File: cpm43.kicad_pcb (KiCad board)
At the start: 2 copper layers, 232.2 x 76.7 mm, 185 parts, among them Q1 Q_NPN_BCE, SW1 SW_PUSH, U1 ATmega32U4, U2 PRTR5V0U2X

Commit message: Tact switch
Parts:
- SW1: footprint Keebio-Parts:CandK_6x6mm_Tactile -> Buttons_Switches_SMD:SW_SPST_TL3342
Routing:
- net GND: track 114.4 -> 120.7 mm, vias 167 -> 169
- net RST: track 178.8 -> 181.2 mm, vias 5 -> 7
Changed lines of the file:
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@@
     (thickness 1.6)
     (drawings 49)
-    (tracks 2415)
+    (tracks 2423)
     (zones 0)
     (modules 185)
@@
     (add_net VCC)
   )
+  (module Buttons_Switches_SMD:SW_SPST_TL3342 (layer B.Cu)
+    (at 233.3244 85.852 270)
+    (descr "Low-profile SMD Tactile Switch, https://www.e-switch.com/system/asset/product_line/data_sheet/165/TL3342.pdf")
+    (tags "SPST Tactile Switch")
+    (attr smd)
+    (fp_text reference SW1 (at 0 3.75 270) (layer B.SilkS)
+      (effects (font (size 1 1) (thickness 0.15)) (justify mirror))
+    )
+    (fp_text value SW_PUSH (at 0 -3.75 270) (layer B.Fab)
+      (effects (font (size 1 1) (thickness 0.15)) (justify mirror))
+    )
+    (fp_text user %R (at 0 3.75 270) (layer B.Fab)
+      (effects (font (size 1 1) (thickness 0.15)) (justify mirror))
+    )
+    (fp_line (start 3.2 -2.1) (end 3.2 -1.6) (layer B.Fab) (width 0.1))
+    (fp_line (start 3.2 2.1) (end 3.2 1.6) (layer B.Fab) (width 0.1))
+    (fp_line (start -3.2 -2.1) (end -3.2 -1.6) (layer B.Fab) (width 0.1))
+    (fp_line (start -3.2 2.1) (end -3.2 1.6) (layer B.Fab) (width 0.1))
+    (fp_line (start 2.7 2.1) (end 2.7 1.6) (layer B.Fab) (width 0.1))
+    (fp_line (start 1.7 2.1) (end 3.2 2.1) (layer B.Fab) (width 0.1))
+    (fp_line (start 3.2 1.6) (end 2.2 1.6) (layer B.Fab) (width 0.1))
+    (fp_line (start -2.7 2.1) (end -2.7 1.6) (layer B.Fab) (width 0.1))
+    (fp_line (start -1.7 2.1) (end -3.2 2.1) (layer B.Fab) (width 0.1))
+    (fp_line (start -3.2 1.6) (end -2.2 1.6) (layer B.Fab) (width 0.1))
+    (fp_line (start -2.7 -2.1) (end -2.7 -1.6) (layer B.Fab) (width 0.1))
+    (fp_line (start -3.2 -1.6) (end -2.2 -1.6) (layer B.Fab) (width 0.1))
+    (fp_line (start -1.7 -2.1) (end -3.2 -2.1) (layer B.Fab) (width 0.1))
+    (fp_line (start 1.7 -2.1) (end 3.2 -2.1) (layer B.Fab) (width 0.1))
+    (fp_line (start 2.7 -2.1) (end 2.7 -1.6) (layer B.Fab) (width 0.1))
+    (fp_line (start 3.2 -1.6) (end 2.2 -1.6) (layer B.Fab) (width 0.1))
+    (fp_line (start -1.7 -2.3) (end -1.25 -2.75) (layer B.SilkS) (width 0.12))
+    (fp_line (start 1.7 -2.3) (end 1.25 -2.75) (layer B.SilkS) (width 0.12))
+    (fp_line (start 1.7 2.3) (end 1.25 2.75) (layer B.SilkS) (width 0.12))
+    (fp_line (start -1.7 2.3) (end -1.25 2.75) (layer B.SilkS) (width 0.12))
+    (fp_line (start -2 1) (end -1 2) (layer B.Fab) (width 0.1))
+    (fp_line (start -1 2) (end 1 2) (layer B.Fab) (width 0.1))
+    (fp_line (start 1 2) (end 2 1) (layer B.Fab) (width 0.1))
+    (fp_line (start 2 1) (end 2 -1) (layer B.Fab) (width 0.1))
+    (fp_line (start 2 -1) (end 1 -2) (layer B.Fab) (width 0.1))
+    (fp_line (start 1 -2) (end -1 -2) (layer B.Fab) (width 0.1))
+    (fp_line (start -1 -2) (end -2 -1) (layer B.Fab) (width 0.1))
+    (fp_line (start -2 -1) (end -2 1) (layer B.Fab) (width 0.1))
+    (fp_line (start 2.75 1) (end 2.75 -1) (layer B.SilkS) (width 0.12))
+    (fp_line (start -1.25 -2.75) (end 1.25 -2.75) (layer B.SilkS) (width 0.12))
+    (fp_line (start -2.75 1) (end -2.75 -1) (layer B.SilkS) (width 0.12))
+    (fp_line (start -1.25 2.75) (end 1.25 2.75) (layer B.SilkS) (width 0.12))
+    (fp_line (start -2.6 1.2) (end -2.6 -1.2) (layer B.Fab) (width 0.1))
+    (fp_line (start -2.6 -1.2) (end -1.2 -2.6) (layer B.Fab) (width 0.1))
+    (fp_line (start -1.2 -2.6) (end 1.2 -2.6) (layer B.Fab) (width 0.1))
+    (fp_line (start 1.2 -2.6) (end 2.6 -1.2) (layer B.Fab) (width 0.1))
+    (fp_line (start 2.6 -1.2) (end 2.6 1.2) (layer B.Fab) (width 0.1))
+    (fp_line (start 2.6 1.2) (end 1.2 2.6) (layer B.Fab) (width 0.1))
+    (fp_line (start 1.2 2.6) (end -1.2 2.6) (layer B.Fab) (width 0.1))
+    (fp_line (start -1.2 2.6) (end -2.6 1.2) (layer B.Fab) (width 0.1))
+    (fp_line (start -4.25 3) (end 4.25 3) (layer B.CrtYd) (width 0.05))
+    (fp_line (start 4.25 3) (end 4.25 -3) (layer B.CrtYd) (width 0.05))
+    (fp_line (start 4.25 -3) (end -4.25 -3) (layer B.CrtYd) (width 0.05))
+    (fp_line (start -4.25 -3) (end -4.25 3) (layer B.CrtYd) (width 0.05))
+    (fp_circle (center 0 0) (end 1 0) (layer B.Fab) (width 0.1))
+    (pad 1 smd rect (at -3.15 1.9 270) (size 1.7 1) (layers B.Cu B.Paste B.Mask)
+      (net 2 GND))
+    (pad 1 smd rect (at 3.15 1.9 270) (size 1.7 1) (layers B.Cu B.Paste B.Mask)
+      (net 2 GND))
+    (pad 2 smd rect (at -3.15 -1.9 270) (size 1.7 1) (layers B.Cu B.Paste B.Mask)
+      (net 126 RST))
+    (pad 2 smd rect (at 3.15 -1.9 270) (size 1.7 1) (layers B.Cu B.Paste B.Mask)
+      (net 126 RST))
+    (model ${KISYS3DMOD}/Buttons_Switches_SMD.3dshapes/SW_SPST_TL3342.wrl
+      (at (xyz 0 0 0))
+      (scale (xyz 1 1 1))
+      (rotate (xyz 0 0 0))
+    )
+  )
   (module keyboard_parts:Pin_Header_Straight_2x03_Pitch2.54mm (layer F.Cu)
     (at 128.1176 118.7958 90)
@@
     )
   )
-  (module Keebio-Parts:CandK_6x6mm_Tactile (layer B.Cu)
-    (at 233.3244 85.852 270)
-    (fp_text reference SW1 (at -4.699 -0.0635 90) (layer B.SilkS)
-      (effects (font (size 1 1) (thickness 0.15)) (justify mirror))
-    )
-    (fp_text value SW_PUSH (at 0 4.75 270) (layer B.Fab)
-      (effects (font (size 1 1) (thickness 0.15)) (justify mirror))
-    )
-    (fp_circle (center 0 0) (end 1.75 0) (layer B.SilkS) (width 0.15))
-    (fp_line (start 0 3) (end -3 3) (layer B.SilkS) (width 0.15))
-    (fp_line (start -3 3) (end -3 -3) (layer B.SilkS) (width 0.15))
-    (fp_line (start -3 -3) (end 3 -3) (layer B.SilkS) (width 0.15))
-    (fp_line (start 3 -3) (end 3 3) (layer B.SilkS) (width 0.15))
-    (fp_line (start 3 3) (end 0 3) (layer B.SilkS) (width 0.15))
-    (pad 4 smd rect (at 4.75 -2.25 270) (size 1.54 1.3) (layers B.Cu B.Paste B.Mask))
-    (pad 2 smd rect (at 4.75 2.25 270) (size 1.55 1.3) (layers B.Cu B.Paste B.Mask)
-      (net 126 RST))
-    (pad 1 smd rect (at -4.75 2.25 270) (size 1.55 1.3) (layers B.Cu B.Paste B.Mask)
-      (net 2 GND))
-    (pad 3 smd rect (at -4.75 -2.25 270) (size 1.55 1.3) (layers B.Cu B.Paste B.Mask))
-    (model "${KIPRJMOD}/3D/Tact Switch SMD 6x6mm.stp"
-      (at (xyz 0 0 0))
-      (scale (xyz 1 1 1))
-      (rotate (xyz 0 0 0))
-    )
-  )
   (module keyboard_parts:QFP44 locked (layer B.Cu)
     (at 109.093 126.238 270)
@@
   (gr_line (start 119.888 60.071) (end 183.642 56.769) (layer B.Fab) (width 0.2))
   (gr_line (start 115.824 70.358) (end 119.888 60.071) (layer B.Fab) (width 0.2))
+  (via (at 235.23448 82.64144) (size 0.6) (drill 0.3) (layers F.Cu B.Cu) (net 126))
   (segment (start 109.8931 120.523) (end 109.8931 121.0818) (width 0.2032) (layer B.Cu) (net 1))
   (segment (start 102.975 120.015) (end 102.85 120.015) (width 0.2032) (layer B.Cu) (net 1))
@@
   (segment (start 116.45932 117.55596) (end 116.38534 117.55596) (width 0.127) (layer B.Cu) (net 2))
   (segment (start 117.40642 116.65458) (end 116.45932 117.55596) (width 0.127) (layer B.Cu) (net 2))
+  (via (at 231.4244 89.002) (size 0.6) (drill 0.3) (layers F.Cu B.Cu) (net 2))
+  (via (at 231.4244 82.702) (size 0.6) (drill 0.3) (layers F.Cu B.Cu) (net 2))
+  (segment (start 231.4244 89.002) (end 231.4244 82.702) (width 0.127) (layer F.Cu) (net 2))
   (segment (start 109.093 118.257) (end 109.875 117.475) (width 0.127) (layer B.Cu) (net 3))
   (segment (start 109.093 120.523) (end 109.093 118.257) (width 0.127) (layer B.Cu) (net 3))
@@
   (via (at 233.045 87.884) (size 0.6) (drill 0.3) (layers F.Cu B.Cu) (net 126))
   (segment (start 233.085 87.844) (end 233.045 87.884) (width 0.127) (layer B.Cu) (net 126))
-  (segment (start 237.7948 87.844) (end 233.085 87.844) (width 0.127) (layer B.Cu) (net 126))
   (via (at 122.789855 97.198886) (size 0.6) (drill 0.3) (layers F.Cu B.Cu) (net 126))
   (segment (start 123.089854 96.898887) (end 122.789855 97.198886) (width 0.127) (layer B.Cu) (net 126))
@@
   (segment (start 225.412289 95.689431) (end 226.55784 94.54388) (width 0.127) (layer B.Cu) (net 126))
   (segment (start 233.045 87.884) (end 233.045 94.54388) (width 0.127) (layer F.Cu) (net 126))
-  (segment (start 233.045 87.884) (end 232.3338 87.1728) (width 0.127) (layer B.Cu) (net 126))
-  (segment (start 232.3338 87.1728) (end 232.0544 87.1728) (width 0.127) (layer B.Cu) (net 126))
-  (segment (start 231.0744 88.1528) (end 231.0744 90.602) (width 0.127) (layer B.Cu) (net 126))
-  (segment (start 232.0544 87.1728) (end 231.0744 88.1528) (width 0.127) (layer B.Cu) (net 126))
   (segment (start 237.7948 87.844) (end 238.506 87.844) (width 0.127) (layer B.Cu) (net 126))
   (segment (start 122.809 97.218031) (end 122.789855 97.198886) (width 0.127) (layer F.Cu) (net 126))
@@
   (segment (start 133.1976 118.7958) (end 131.9276 117.5258) (width 0.127) (layer B.Cu) (net 126))
   (segment (start 131.9276 117.5258) (end 131.9276 115.443) (width 0.127) (layer B.Cu) (net 126))
+  (segment (start 235.2294 88.02) (end 235.2294 87.844) (width 0.127) (layer B.Cu) (net 126))
+  (segment (start 235.2244 88.025) (end 235.2294 88.02) (width 0.127) (layer B.Cu) (net 126))
+  (segment (start 235.2244 89.002) (end 235.2244 88.98636) (width 0.127) (layer B.Cu) (net 126))
+  (segment (start 237.7948 87.844) (end 235.2294 87.844) (width 0.127) (layer B.Cu) (net 126))
+  (segment (start 235.2294 87.844) (end 233.085 87.844) (width 0.127) (layer B.Cu) (net 126))
+  (segment (start 235.2244 88.98636) (end 235.2244 88.025) (width 0.127) (layer B.Cu) (net 126))
+  (via (at 235.2244 88.98636) (size 0.6) (drill 0.3) (layers F.Cu B.Cu) (net 126))
+  (segment (start 235.23448 88.97628) (end 235.2244 88.98636) (width 0.127) (layer F.Cu) (net 126))
+  (segment (start 235.23448 82.64144) (end 235.23448 88.97628) (width 0.127) (layer F.Cu) (net 126))
   (segment (start 105.0925 131.953) (end 105.0925 132.5118) (width 0.127) (layer B.Cu) (net 127))
   (segment (start 105.0925 132.5118) (end 104.655611 132.948689) (width 0.127) (layer B.Cu) (net 127))

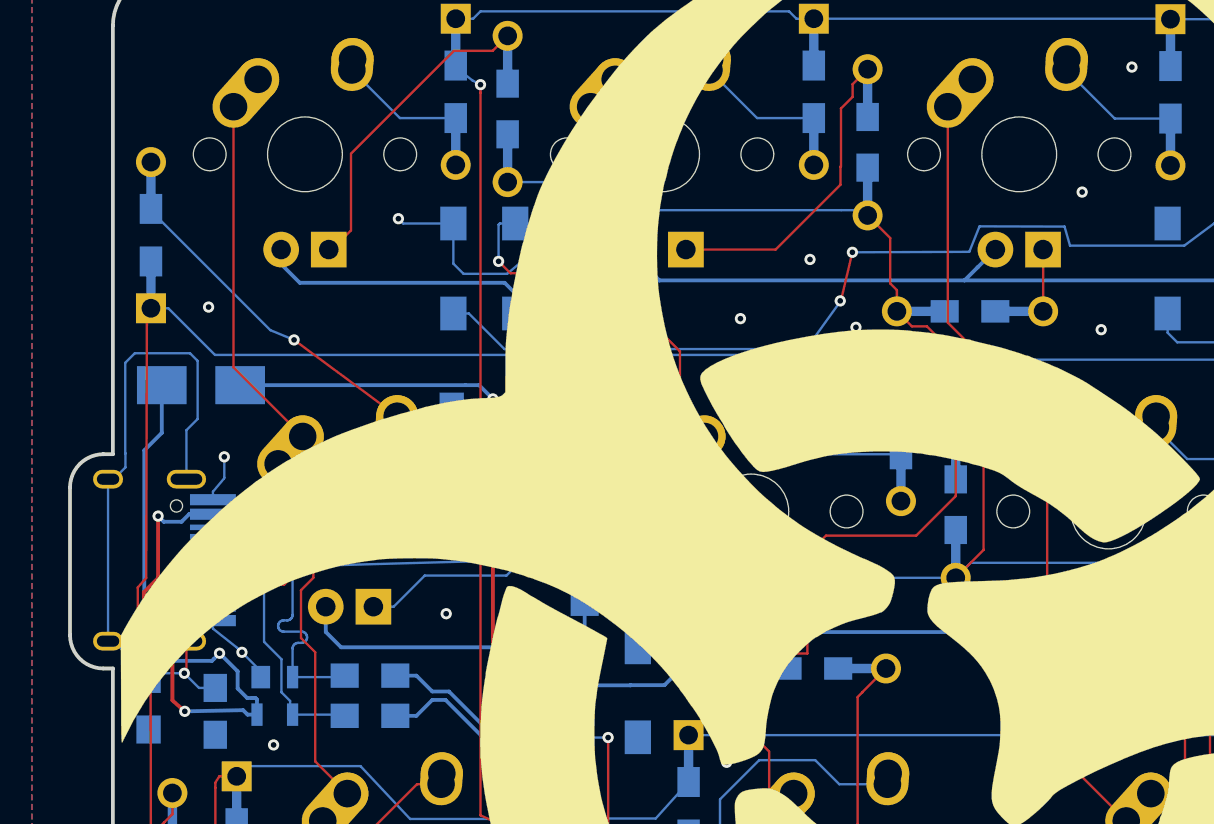
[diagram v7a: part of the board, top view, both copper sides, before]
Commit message: Added usb breakout header
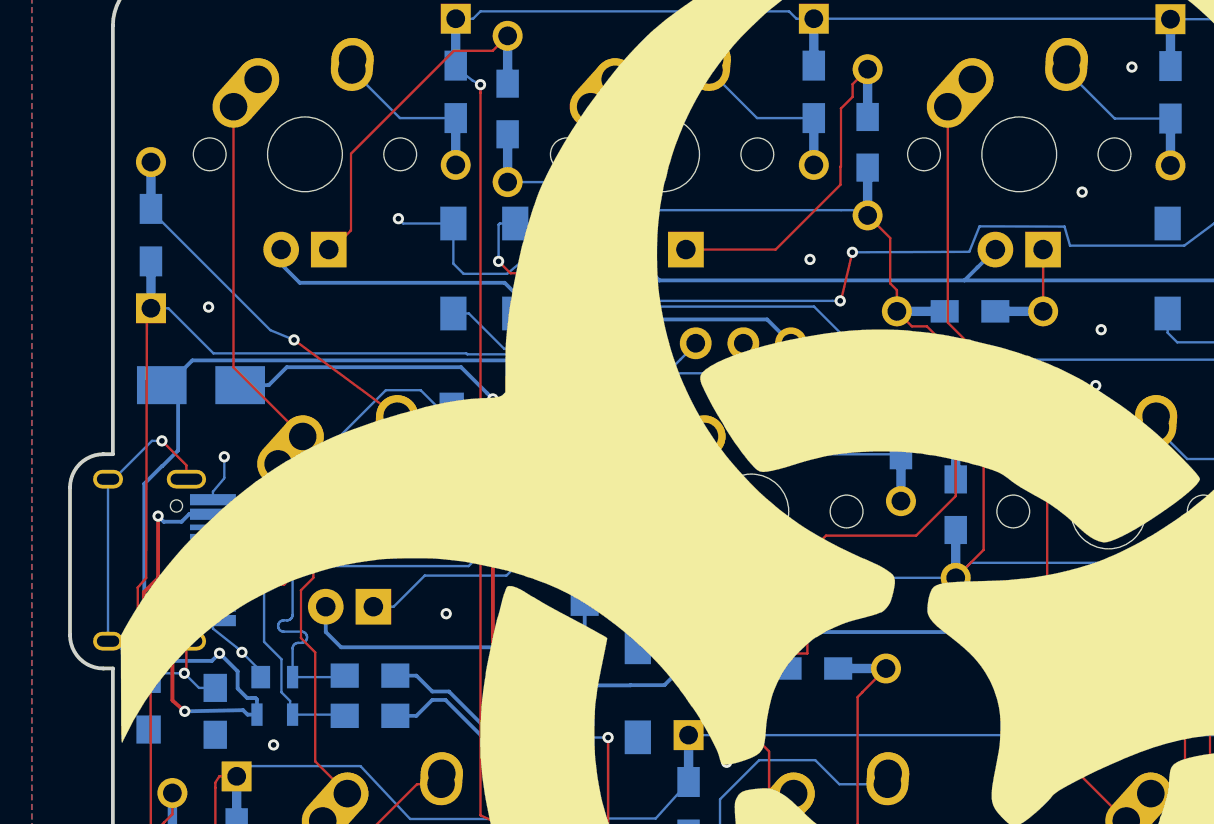
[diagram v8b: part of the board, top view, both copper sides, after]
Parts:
- added J1: Conn_01x04, Pin_Headers:Pin_Header_Straight_1x04_Pitch2.54mm, B.Cu at (61.8, 79.9)
- C1: value 0.1uF -> 0.1uf
- C4: value 0.1uF -> 4.7uF
- X1: value (none) -> Crystal_GND24
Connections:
- LED14 pad 2: Net-(LED14-Pad2) -> (no net)
- U1 pad 28: Net-(U1-Pad28) -> (no net)
- U1 pad 36: Net-(U1-Pad36) -> (no net)
- U1 pad 37: Net-(U1-Pad37) -> (no net)
- U1 pad 42: Net-(U1-Pad42) -> (no net)
- U1 pad 8: Net-(U1-Pad8) -> (no net)
- USB1 pad 3: Net-(USB1-Pad3) -> (no net)
- USB1 pad 9: Net-(USB1-Pad9) -> (no net)
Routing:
- net VCC: track 46.3 -> 82.2 mm
- net Net-(J1-Pad3): track 17.5 -> 49.6 mm
- net Net-(J1-Pad2): track 17.5 -> 48.8 mm, vias 0 -> 2
- net Net-(C7-Pad2): track 35.1 -> 23.8 mm, vias 1 -> 2
- net ROW1: track 359.8 -> 361.9 mm
- net COL1: track 112.0 -> 113.2 mm
- net +5V: track 1188.6 -> 1189.4 mm
- net GND: vias 169 -> 170
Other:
- board text added: "D+"
- board text added: "D-"
- board text added: "VCC"
